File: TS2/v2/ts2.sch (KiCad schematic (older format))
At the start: 7 parts, among them U10 74LS32, U4 74LS06, U7 74LS08

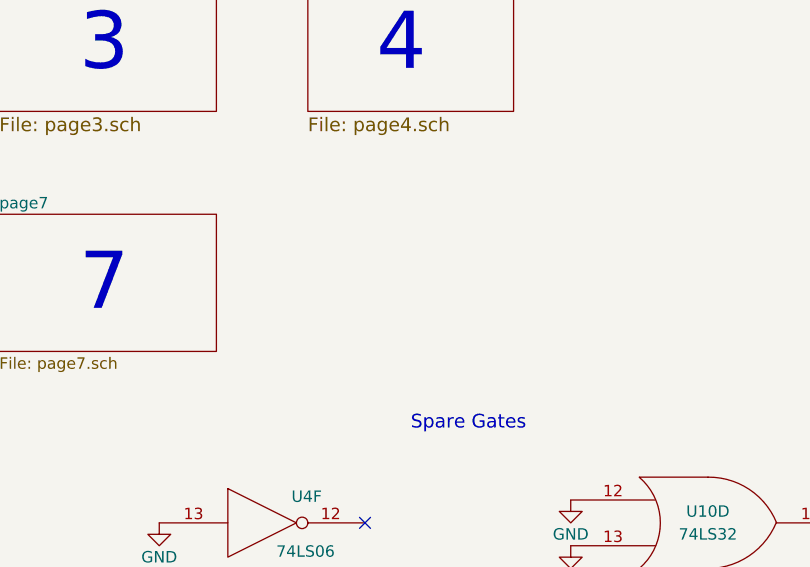
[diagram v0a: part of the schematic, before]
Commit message: Add interrupt control circuitry.
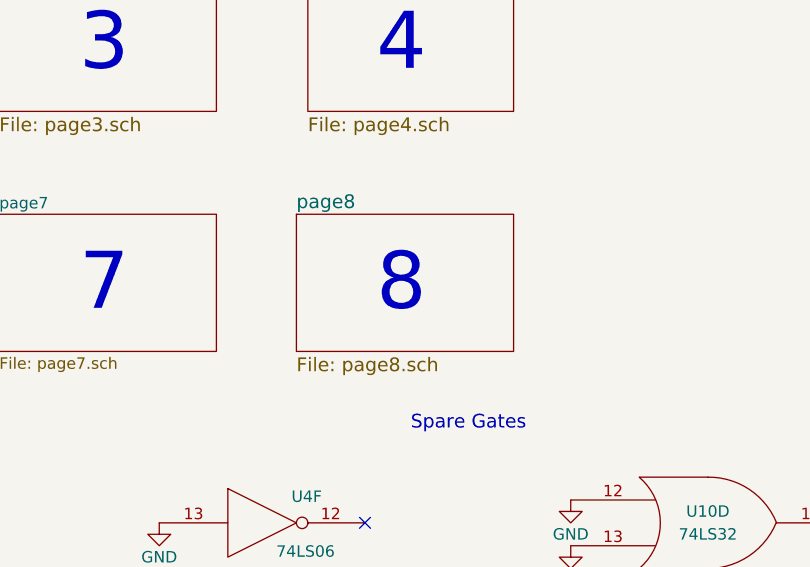
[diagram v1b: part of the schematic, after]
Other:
- note added: "8"
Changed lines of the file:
@@
 $Descr A 11000 8500
 encoding utf-8
-Sheet 1 8
+Sheet 1 9
 Title "TS2 68000 Single Board Computer"
-Date "2016-12-04"
+Date "2016-12-11"
 Rev "2.0"
 Comp "Jeff Tranter"
@@
 	1    0    0    -1
 $EndComp
+$Sheet
+S 6000 3250 950  600
+U 584DB98F
+F0 "page8" 60
+F1 "page8.sch" 60
+$EndSheet
+Text Notes 6350 3700 0    250  ~ 0
+8
 $EndSCHEMATC

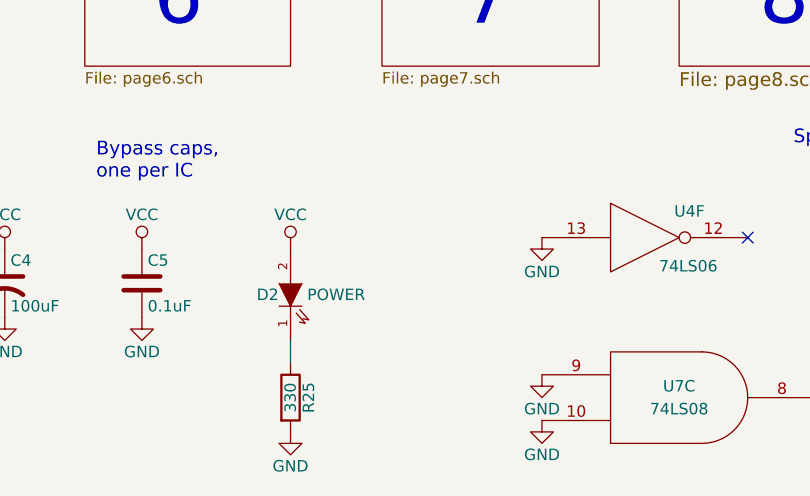
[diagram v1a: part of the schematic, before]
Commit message: Add power protection diode. Add table of power pins for ICs to BOM.
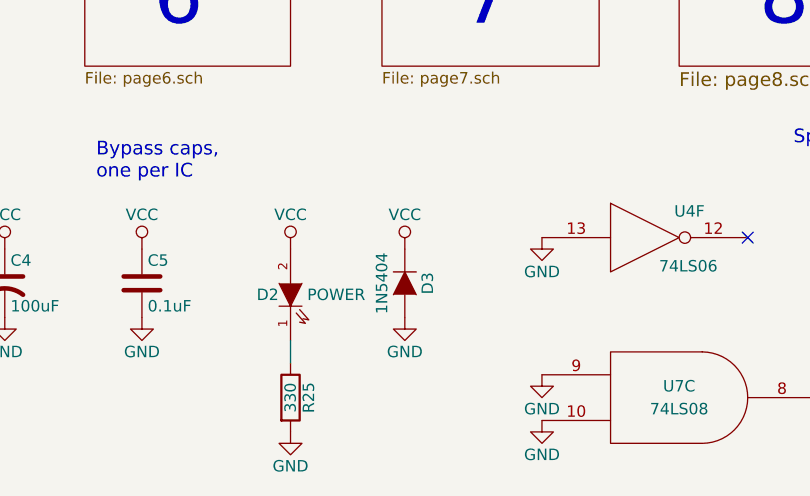
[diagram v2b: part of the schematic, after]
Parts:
- added D3: 1N5404, symbol D
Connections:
- net GND: now also D3.2 (A)
- net VCC: now also D3.1 (K)
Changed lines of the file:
@@
 Text Notes 6350 3700 0    250  ~ 0
 8
+$Comp
+L D D3
+U 1 1 585E8EAF
+P 4800 4800
+F 0 "D3" H 4800 4900 50  0000 C CNN
+F 1 "1N5404" H 4800 4700 50  0000 C CNN
+F 2 "" H 4800 4800 50  0000 C CNN
+F 3 "" H 4800 4800 50  0000 C CNN
+	1    4800 4800
+	0    1    1    0
+$EndComp
+$Comp
+L VCC #PWR?
+U 1 1 585E8EEE
+P 4800 4650
+F 0 "#PWR?" H 4800 4500 50  0001 C CNN
+F 1 "VCC" H 4800 4800 50  0000 C CNN
+F 2 "" H 4800 4650 50  0000 C CNN
+F 3 "" H 4800 4650 50  0000 C CNN
+	1    4800 4650
+	1    0    0    -1
+$EndComp
+$Comp
+L GND #PWR?
+U 1 1 585E8F6D
+P 4800 4950
+F 0 "#PWR?" H 4800 4700 50  0001 C CNN
+F 1 "GND" H 4800 4800 50  0000 C CNN
+F 2 "" H 4800 4950 50  0000 C CNN
+F 3 "" H 4800 4950 50  0000 C CNN
+	1    4800 4950
+	1    0    0    -1
+$EndComp
 $EndSCHEMATC

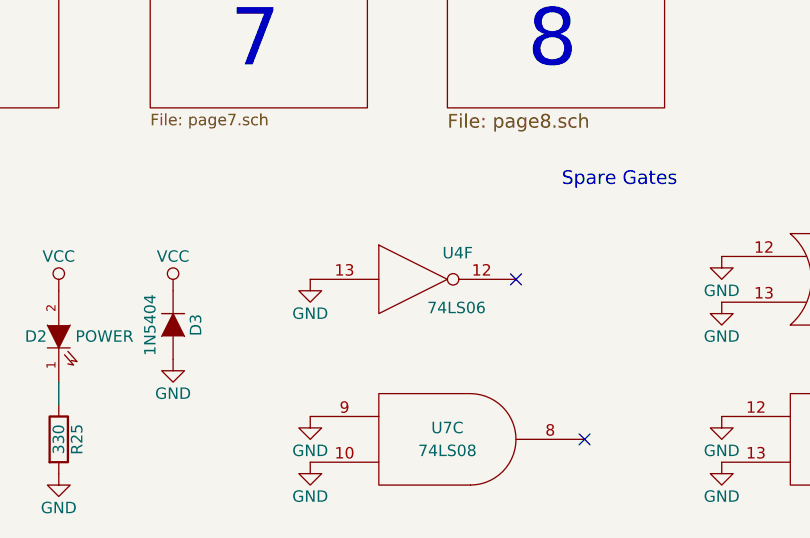
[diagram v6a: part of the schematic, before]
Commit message: Implementing more of interrupt circuitry.
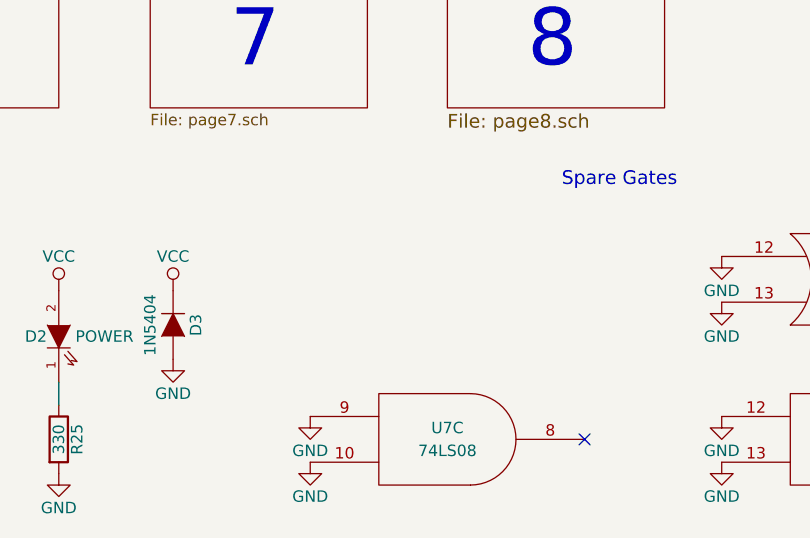
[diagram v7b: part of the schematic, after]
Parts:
- removed U4: 74LS06, symbol 74LS06
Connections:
- no-connect marks 4 -> 3
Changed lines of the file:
@@
 Spare Gates
-$Comp
-L 74LS06 U4
-U 6 1 58430894
-P 5850 4600
-F 0 "U4" H 6045 4715 50  0000 C CNN
-F 1 "74LS06" H 6040 4475 50  0000 C CNN
-F 2 "" H 5850 4600 50  0000 C CNN
-F 3 "" H 5850 4600 50  0000 C CNN
-	6    5850 4600
-	1    0    0    -1
-$EndComp
 $Comp
 L 74LS08 U7
@@
 NoConn ~ 8400 5300
 NoConn ~ 6600 5300
-NoConn ~ 6300 4600
 $Comp
 L GND #PWR011
-U 1 1 58432036
-P 5400 4600
-F 0 "#PWR011" H 5400 4350 50  0001 C CNN
-F 1 "GND" H 5400 4450 50  0000 C CNN
-F 2 "" H 5400 4600 50  0000 C CNN
-F 3 "" H 5400 4600 50  0000 C CNN
-	1    5400 4600
-	1    0    0    -1
-$EndComp
-$Comp
-L GND #PWR012
 U 1 1 584320D8
 P 5400 5200
-F 0 "#PWR012" H 5400 4950 50  0001 C CNN
+F 0 "#PWR011" H 5400 4950 50  0001 C CNN
 F 1 "GND" H 5400 5050 50  0000 C CNN
 F 2 "" H 5400 5200 50  0000 C CNN
@@
 $EndComp
 $Comp
-L GND #PWR013
+L GND #PWR012
 U 1 1 584320FC
 P 5400 5400
-F 0 "#PWR013" H 5400 5150 50  0001 C CNN
+F 0 "#PWR012" H 5400 5150 50  0001 C CNN
 F 1 "GND" H 5400 5250 50  0000 C CNN
 F 2 "" H 5400 5400 50  0000 C CNN
@@
 $EndComp
 $Comp
-L GND #PWR014
+L GND #PWR013
 U 1 1 584321C8
 P 7200 4500
-F 0 "#PWR014" H 7200 4250 50  0001 C CNN
+F 0 "#PWR013" H 7200 4250 50  0001 C CNN
 F 1 "GND" H 7200 4350 50  0000 C CNN
 F 2 "" H 7200 4500 50  0000 C CNN
@@
 $EndComp
 $Comp
-L GND #PWR015
+L GND #PWR014
 U 1 1 584321EC
 P 7200 4700
-F 0 "#PWR015" H 7200 4450 50  0001 C CNN
+F 0 "#PWR014" H 7200 4450 50  0001 C CNN
 F 1 "GND" H 7200 4550 50  0000 C CNN
 F 2 "" H 7200 4700 50  0000 C CNN
@@
 $EndComp
 $Comp
-L GND #PWR016
+L GND #PWR015
 U 1 1 58432210
 P 7200 5200
-F 0 "#PWR016" H 7200 4950 50  0001 C CNN
+F 0 "#PWR015" H 7200 4950 50  0001 C CNN
 F 1 "GND" H 7200 5050 50  0000 C CNN
 F 2 "" H 7200 5200 50  0000 C CNN
@@
 $EndComp
 $Comp
-L GND #PWR017
+L GND #PWR016
 U 1 1 58432234
 P 7200 5400
-F 0 "#PWR017" H 7200 5150 50  0001 C CNN
+F 0 "#PWR016" H 7200 5150 50  0001 C CNN
 F 1 "GND" H 7200 5250 50  0000 C CNN
 F 2 "" H 7200 5400 50  0000 C CNN
@@
 $EndComp
 $Comp
-L VCC #PWR018
+L VCC #PWR017
 U 1 1 585E8EEE
 P 4800 4650
-F 0 "#PWR018" H 4800 4500 50  0001 C CNN
+F 0 "#PWR017" H 4800 4500 50  0001 C CNN
 F 1 "VCC" H 4800 4800 50  0000 C CNN
 F 2 "" H 4800 4650 50  0000 C CNN
@@
 $EndComp
 $Comp
-L GND #PWR019
+L GND #PWR018
 U 1 1 585E8F6D
 P 4800 4950
-F 0 "#PWR019" H 4800 4700 50  0001 C CNN
+F 0 "#PWR018" H 4800 4700 50  0001 C CNN
 F 1 "GND" H 4800 4800 50  0000 C CNN
 F 2 "" H 4800 4950 50  0000 C CNN

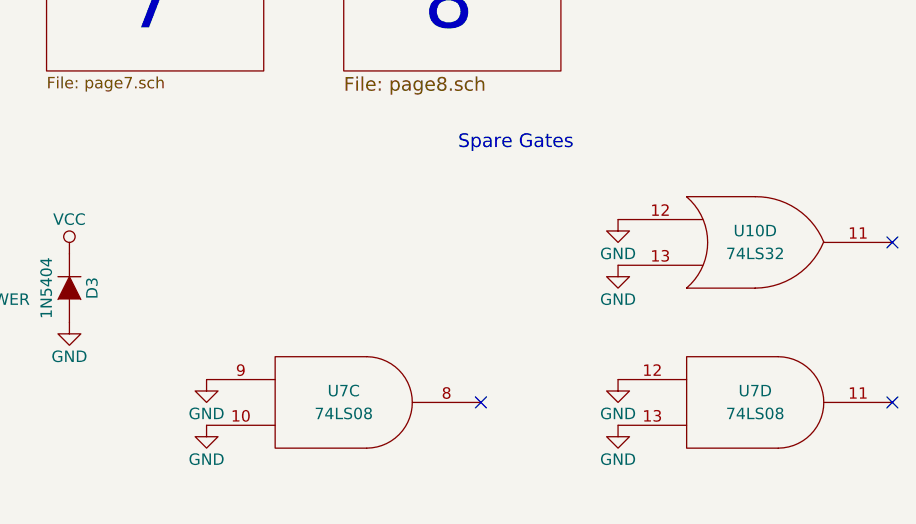
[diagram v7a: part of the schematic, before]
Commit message: Corrections to interrupt circuitry.
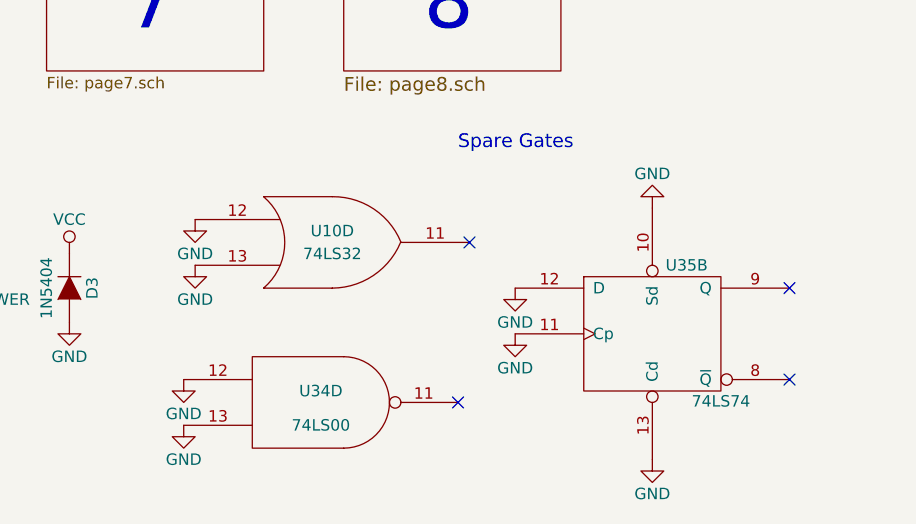
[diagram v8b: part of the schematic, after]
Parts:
- removed U7: 74LS08, symbol 74LS08
- added U34: 74LS00, symbol 74LS00
- added U35: 74LS74, symbol 74LS74
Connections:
- net GND: now also U34.12, U34.13, U34.7 (GND), U35.10 (Sd), U35.11 (Cp), U35.12 (D), U35.13 (Cd), U35.7 (GND)
- net VCC: now also U34.14 (VCC), U35.14 (VCC)
- no-connect marks 3 -> 4
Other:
- moved on the sheet: U10D
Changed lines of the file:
@@
 Spare Gates
-$Comp
-L 74LS08 U7
-U 3 1 58430C38
-P 6000 5300
-F 0 "U7" H 6000 5350 50  0000 C CNN
-F 1 "74LS08" H 6000 5250 50  0000 C CNN
-F 2 "" H 6000 5300 50  0000 C CNN
-F 3 "" H 6000 5300 50  0000 C CNN
-	3    6000 5300
-	1    0    0    -1
-$EndComp
-$Comp
-L 74LS08 U7
-U 4 1 58430C82
-P 7800 5300
-F 0 "U7" H 7800 5350 50  0000 C CNN
-F 1 "74LS08" H 7800 5250 50  0000 C CNN
-F 2 "" H 7800 5300 50  0000 C CNN
-F 3 "" H 7800 5300 50  0000 C CNN
-	4    7800 5300
-	1    0    0    -1
-$EndComp
 $Comp
 L 74LS32 U10
 U 4 1 5843109B
-P 7800 4600
-F 0 "U10" H 7800 4650 50  0000 C CNN
-F 1 "74LS32" H 7800 4550 50  0000 C CNN
-F 2 "" H 7800 4600 50  0000 C CNN
-F 3 "" H 7800 4600 50  0000 C CNN
-	4    7800 4600
+P 5950 4600
+F 0 "U10" H 5950 4650 50  0000 C CNN
+F 1 "74LS32" H 5950 4550 50  0000 C CNN
+F 2 "" H 5950 4600 50  0000 C CNN
+F 3 "" H 5950 4600 50  0000 C CNN
+	4    5950 4600
 	1    0    0    -1
 $EndComp
-NoConn ~ 8400 4600
-NoConn ~ 8400 5300
-NoConn ~ 6600 5300
+NoConn ~ 6550 4600
 $Comp
 L GND #PWR011
-U 1 1 584320D8
-P 5400 5200
-F 0 "#PWR011" H 5400 4950 50  0001 C CNN
-F 1 "GND" H 5400 5050 50  0000 C CNN
-F 2 "" H 5400 5200 50  0000 C CNN
-F 3 "" H 5400 5200 50  0000 C CNN
-	1    5400 5200
+U 1 1 584321C8
+P 5350 4500
+F 0 "#PWR011" H 5350 4250 50  0001 C CNN
+F 1 "GND" H 5350 4350 50  0000 C CNN
+F 2 "" H 5350 4500 50  0000 C CNN
+F 3 "" H 5350 4500 50  0000 C CNN
+	1    5350 4500
 	1    0    0    -1
 $EndComp
 $Comp
 L GND #PWR012
-U 1 1 584320FC
-P 5400 5400
-F 0 "#PWR012" H 5400 5150 50  0001 C CNN
-F 1 "GND" H 5400 5250 50  0000 C CNN
-F 2 "" H 5400 5400 50  0000 C CNN
-F 3 "" H 5400 5400 50  0000 C CNN
-	1    5400 5400
-	1    0    0    -1
-$EndComp
-$Comp
-L GND #PWR013
-U 1 1 584321C8
-P 7200 4500
-F 0 "#PWR013" H 7200 4250 50  0001 C CNN
-F 1 "GND" H 7200 4350 50  0000 C CNN
-F 2 "" H 7200 4500 50  0000 C CNN
-F 3 "" H 7200 4500 50  0000 C CNN
-	1    7200 4500
-	1    0    0    -1
-$EndComp
-$Comp
-L GND #PWR014
 U 1 1 584321EC
-P 7200 4700
-F 0 "#PWR014" H 7200 4450 50  0001 C CNN
-F 1 "GND" H 7200 4550 50  0000 C CNN
-F 2 "" H 7200 4700 50  0000 C CNN
-F 3 "" H 7200 4700 50  0000 C CNN
-	1    7200 4700
-	1    0    0    -1
-$EndComp
-$Comp
-L GND #PWR015
-U 1 1 58432210
-P 7200 5200
-F 0 "#PWR015" H 7200 4950 50  0001 C CNN
-F 1 "GND" H 7200 5050 50  0000 C CNN
-F 2 "" H 7200 5200 50  0000 C CNN
-F 3 "" H 7200 5200 50  0000 C CNN
-	1    7200 5200
-	1    0    0    -1
-$EndComp
-$Comp
-L GND #PWR016
-U 1 1 58432234
-P 7200 5400
-F 0 "#PWR016" H 7200 5150 50  0001 C CNN
-F 1 "GND" H 7200 5250 50  0000 C CNN
-F 2 "" H 7200 5400 50  0000 C CNN
-F 3 "" H 7200 5400 50  0000 C CNN
-	1    7200 5400
+P 5350 4700
+F 0 "#PWR012" H 5350 4450 50  0001 C CNN
+F 1 "GND" H 5350 4550 50  0000 C CNN
+F 2 "" H 5350 4700 50  0000 C CNN
+F 3 "" H 5350 4700 50  0000 C CNN
+	1    5350 4700
 	1    0    0    -1
 $EndComp
@@
 $EndComp
 $Comp
-L VCC #PWR017
+L VCC #PWR013
 U 1 1 585E8EEE
 P 4800 4650
-F 0 "#PWR017" H 4800 4500 50  0001 C CNN
+F 0 "#PWR013" H 4800 4500 50  0001 C CNN
 F 1 "VCC" H 4800 4800 50  0000 C CNN
 F 2 "" H 4800 4650 50  0000 C CNN
@@
 $EndComp
 $Comp
-L GND #PWR018
+L GND #PWR014
 U 1 1 585E8F6D
 P 4800 4950
-F 0 "#PWR018" H 4800 4700 50  0001 C CNN
+F 0 "#PWR014" H 4800 4700 50  0001 C CNN
 F 1 "GND" H 4800 4800 50  0000 C CNN
 F 2 "" H 4800 4950 50  0000 C CNN
@@
 	1    0    0    -1
 $EndComp
+$Comp
+L 74LS00 U34
+U 4 1 587B2C0E
+P 5900 5300
+F 0 "U34" H 5900 5350 50  0000 C CNN
+F 1 "74LS00" H 5900 5200 50  0000 C CNN
+F 2 "" H 5900 5300 50  0000 C CNN
+F 3 "" H 5900 5300 50  0000 C CNN
+	4    5900 5300
+	1    0    0    -1
+$EndComp
+$Comp
+L 74LS74 U35
+U 2 1 587B2C8B
+P 7350 5000
+F 0 "U35" H 7500 5300 50  0000 C CNN
+F 1 "74LS74" H 7650 4705 50  0000 C CNN
+F 2 "" H 7350 5000 50  0000 C CNN
+F 3 "" H 7350 5000 50  0000 C CNN
+	2    7350 5000
+	1    0    0    -1
+$EndComp
+$Comp
+L GND #PWR015
+U 1 1 587B30E5
+P 5300 5400
+F 0 "#PWR015" H 5300 5150 50  0001 C CNN
+F 1 "GND" H 5300 5250 50  0000 C CNN
+F 2 "" H 5300 5400 50  0000 C CNN
+F 3 "" H 5300 5400 50  0000 C CNN
+	1    5300 5400
+	1    0    0    -1
+$EndComp
+$Comp
+L GND #PWR016
+U 1 1 587B3109
+P 5300 5200
+F 0 "#PWR016" H 5300 4950 50  0001 C CNN
+F 1 "GND" H 5300 5050 50  0000 C CNN
+F 2 "" H 5300 5200 50  0000 C CNN
+F 3 "" H 5300 5200 50  0000 C CNN
+	1    5300 5200
+	1    0    0    -1
+$EndComp
+NoConn ~ 6500 5300
+$Comp
+L GND #PWR017
+U 1 1 587B3523
+P 6750 4800
+F 0 "#PWR017" H 6750 4550 50  0001 C CNN
+F 1 "GND" H 6750 4650 50  0000 C CNN
+F 2 "" H 6750 4800 50  0000 C CNN
+F 3 "" H 6750 4800 50  0000 C CNN
+	1    6750 4800
+	1    0    0    -1
+$EndComp
+$Comp
+L GND #PWR018
+U 1 1 587B3547
+P 6750 5000
+F 0 "#PWR018" H 6750 4750 50  0001 C CNN
+F 1 "GND" H 6750 4850 50  0000 C CNN
+F 2 "" H 6750 5000 50  0000 C CNN
+F 3 "" H 6750 5000 50  0000 C CNN
+	1    6750 5000
+	1    0    0    -1
+$EndComp
+$Comp
+L GND #PWR019
+U 1 1 587B356B
+P 7350 5550
+F 0 "#PWR019" H 7350 5300 50  0001 C CNN
+F 1 "GND" H 7350 5400 50  0000 C CNN
+F 2 "" H 7350 5550 50  0000 C CNN
+F 3 "" H 7350 5550 50  0000 C CNN
+	1    7350 5550
+	1    0    0    -1
+$EndComp
+$Comp
+L GND #PWR020
+U 1 1 587B358F
+P 7350 4450
+F 0 "#PWR020" H 7350 4200 50  0001 C CNN
+F 1 "GND" H 7350 4300 50  0000 C CNN
+F 2 "" H 7350 4450 50  0000 C CNN
+F 3 "" H 7350 4450 50  0000 C CNN
+	1    7350 4450
+	-1   0    0    1
+$EndComp
+NoConn ~ 7950 4800
+NoConn ~ 7950 5200
 $EndSCHEMATC
